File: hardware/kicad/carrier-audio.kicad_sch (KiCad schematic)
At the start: 4 parts

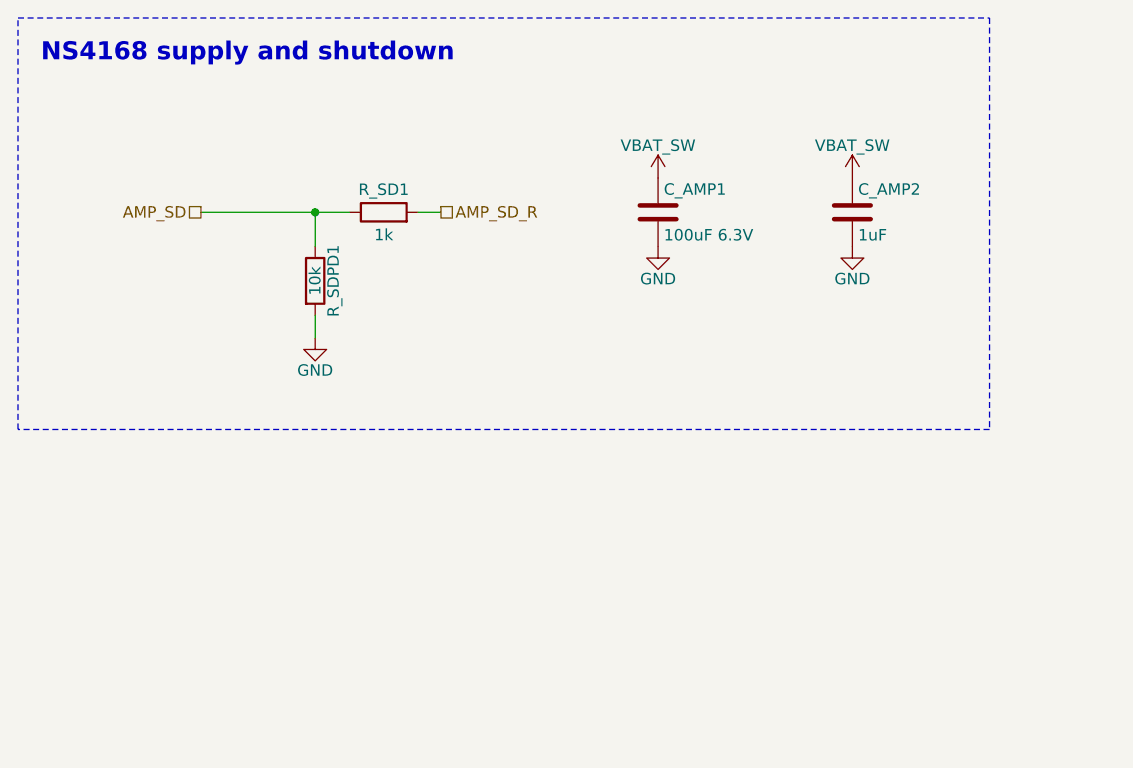
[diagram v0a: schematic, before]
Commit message: hardware: carrier audio sheet draws the whole NS4168, not just its side network
The first pass put U3 on the root beside J_SPK1 and left the audio sheet with R_SD1/R_SDPD1 plus
C_AMP1/C_AMP2 only: a ~15% full A4 page that showed the audio function's side network while the amp
itself sat on the system sheet. That is the split-function failure the migration set out to remove,
and no gate catches it (ERC 0, parity 0, review 0 errors, overlaps 0 all passed).

The whole NS4168 circuit now lives on the audio sheet, laid along its signal path: I2S in on the left,
U3, SPK+/- out on the right to J_SPK1 (which stays on the root so the off-board speaker hangs off it),
AMP_SD entering at the bottom through R_SD1 with R_SDPD1 to GND, and C_AMP1/C_AMP2 beside U3's VDD.
AMP_SD_R is now internal to the sheet. carrier_tme needs no edit: it replaces BLOCKS[1] wholesale, so
U3 simply ceases to exist there and its root no longer has one to drop.

Gates: netlist matches both boards; carrier all + carrier_tme all exit 0 (ERC 0, DRC 0 violations /
0 unconnected / 0 parity, gerbers ok); pcb_diff vs 66bdf5c identical apart from footprint paths
(carrier 25/57 path-changed, carrier_tme 0/73); jlc_bom/jlc_cpl/tme_bom byte-identical; review with
board 0 errors both (5 and 6 warnings, unchanged kinds); audio page now A5 and complete.
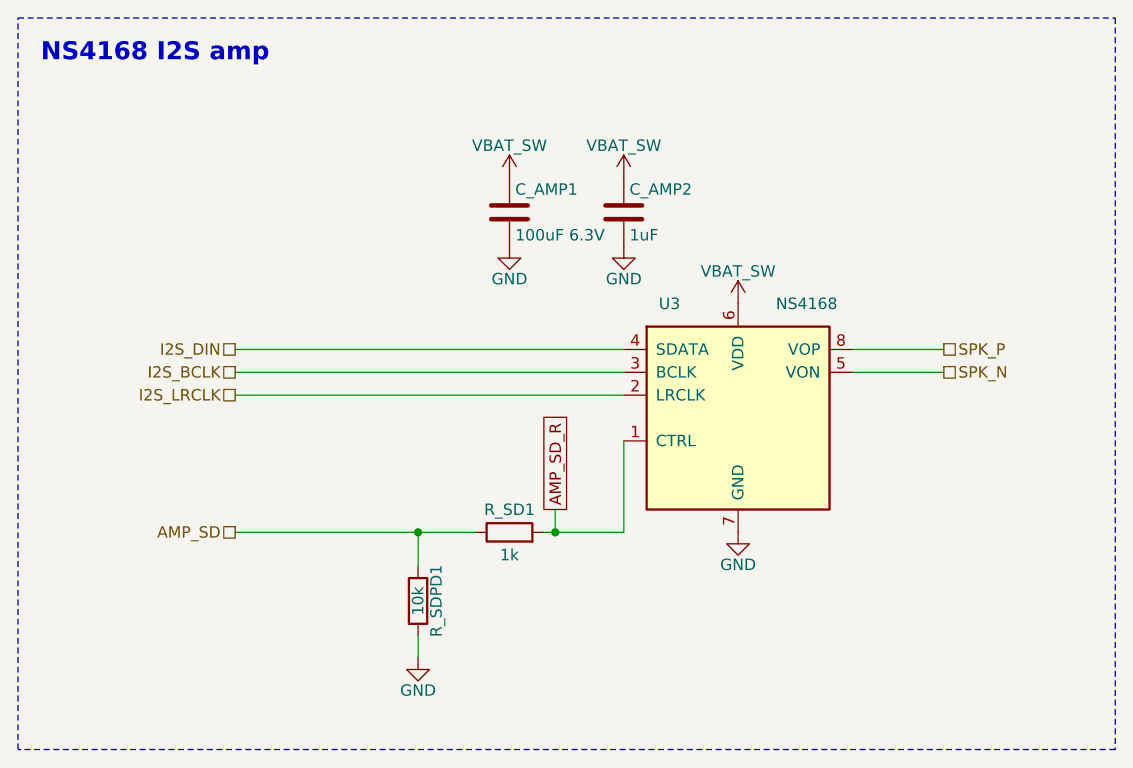
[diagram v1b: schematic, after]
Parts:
- added U3: NS4168, Package_SO:HSOP-8-1EP_3.9x4.9mm_P1.27mm_EP2.3x2.3mm_ThermalVias, symbol local:NS4168
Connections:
- net AMP_SD_R: now also U3.1 (CTRL)
- net GND: now also U3.7 (GND), U3.9 (EP)
- net VBAT_SW: now also U3.6 (VDD)
- new net I2S_BCLK: U3.3 (BCLK)
- new net I2S_DIN: U3.4 (SDATA)
- new net I2S_LRCLK: U3.2 (LRCLK)
- new net SPK_N: U3.5 (VON)
- new net SPK_P: U3.8 (VOP)
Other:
- note added: "NS4168 I2S amp"
- note removed: "NS4168 supply and shutdown"
- title: AirsoftCounter v2 carrier: NS4168 supply and shutdown -> AirsoftCounter v2 carrier: NS4168 I2S amp
- moved on the sheet: C_AMP1, C_AMP2, R_SD1, R_SDPD1
